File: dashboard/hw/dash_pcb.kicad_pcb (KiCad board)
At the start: 2 copper layers, 180 x 65 mm, 5 parts, among them J1 LCD, J2 DEBUG, J3 LCD_BL, U1 LPC11C24FBD48

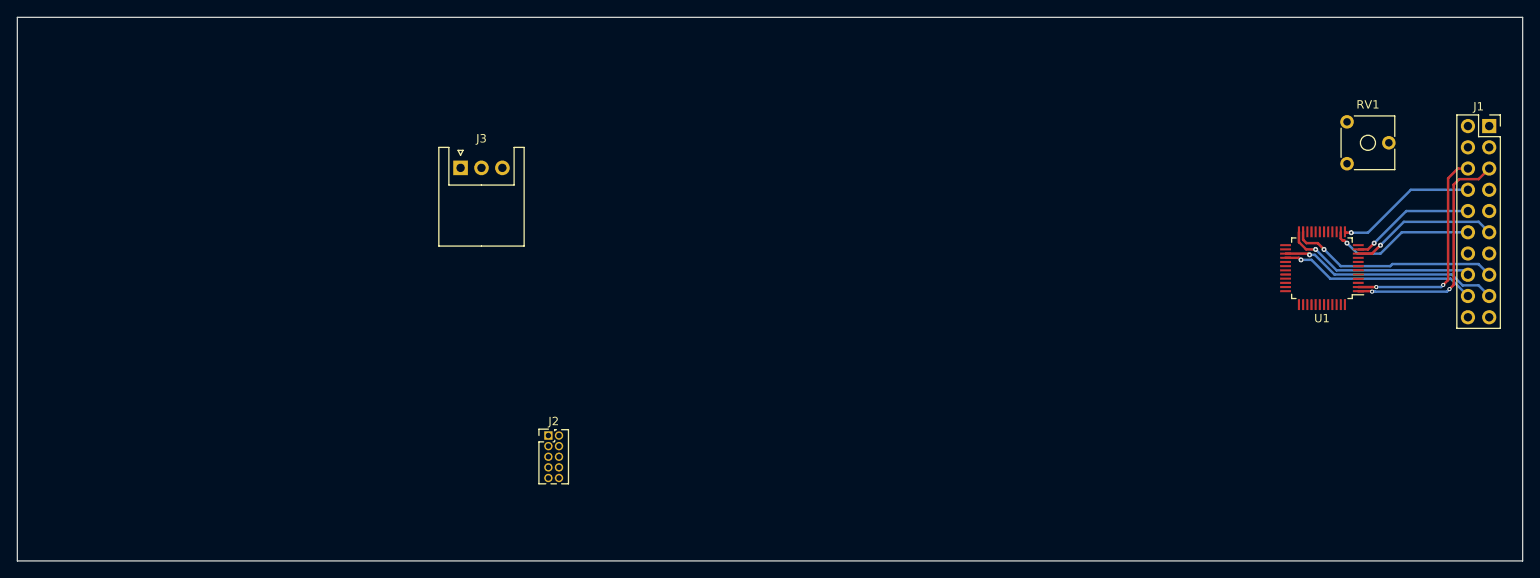
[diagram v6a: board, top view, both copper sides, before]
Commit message: place new components relatively on board
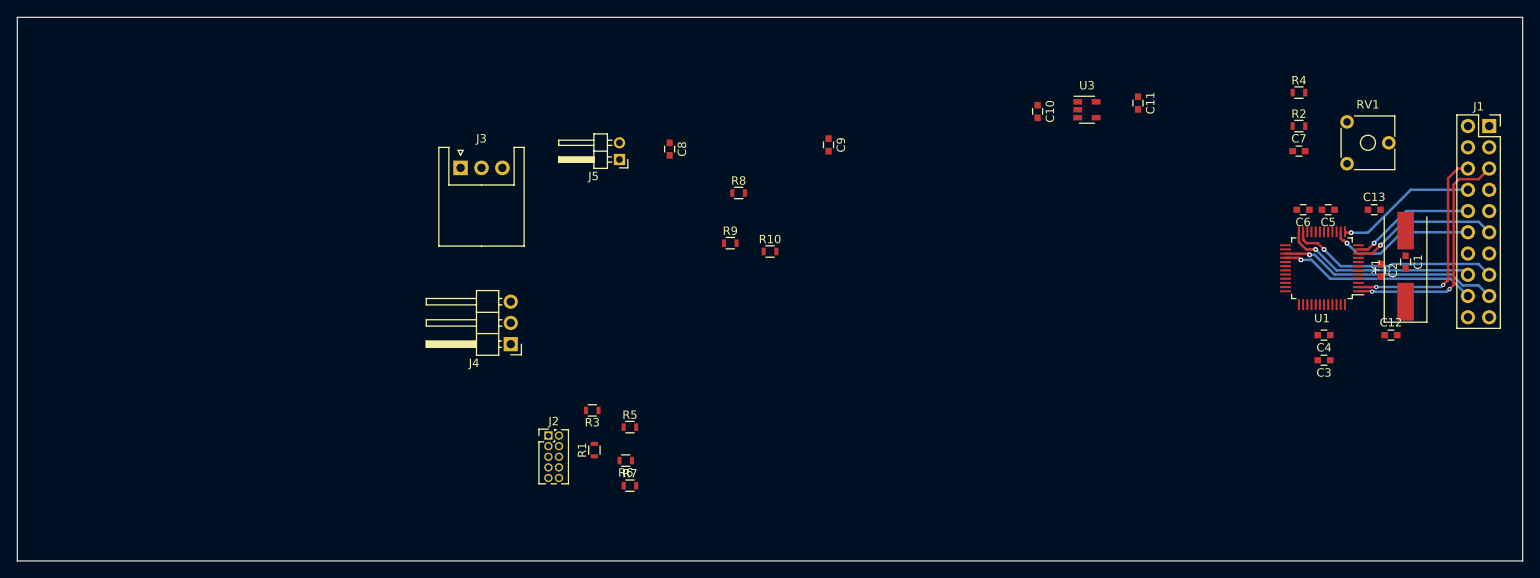
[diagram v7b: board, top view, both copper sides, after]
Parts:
- added C1: 100n, Capacitors_SMD:C_0603, F.Cu at (251.0, 84.2)
- added C10: 2.2u, Capacitors_SMD:C_0603, F.Cu at (207.0, 66.2)
- added C11: 2.2u, Capacitors_SMD:C_0603, F.Cu at (219.0, 65.2)
- added C12: 39p, Capacitors_SMD:C_0603, F.Cu at (249.2, 93.0)
- added C13: 39p, Capacitors_SMD:C_0603, F.Cu at (247.2, 78.0)
- added C2: 10n, Capacitors_SMD:C_0603, F.Cu at (248.0, 85.2)
- added C3: 100n, Capacitors_SMD:C_0603, F.Cu at (241.2, 96.0)
- added C4: 10n, Capacitors_SMD:C_0603, F.Cu at (241.2, 93.0)
- added C5: 10n, Capacitors_SMD:C_0603, F.Cu at (241.8, 78.0)
- added C6: 100n, Capacitors_SMD:C_0603, F.Cu at (238.8, 78.0)
- added C7: 1n, Capacitors_SMD:C_0603, F.Cu at (238.2, 71.0)
- added C8: 2.2u, Capacitors_SMD:C_0603, F.Cu at (163.0, 70.8)
- added C9: 22u, Capacitors_SMD:C_0603, F.Cu at (182.0, 70.2)
- added J4: CAN, Pin_Headers:Pin_Header_Angled_1x03_Pitch2.54mm, F.Cu at (144.0, 94.1)
- added J5: POWER, Pin_Headers:Pin_Header_Angled_1x02_Pitch2.00mm, F.Cu at (157.0, 72.0)
- added R1: 10k, Resistors_SMD:R_0603, F.Cu at (154.0, 106.8)
- added R10: 383k, Resistors_SMD:R_0603, F.Cu at (175.0, 83.0)
- added R2: 60, Resistors_SMD:R_0603, F.Cu at (238.2, 68.0)
- added R3: 10k, Resistors_SMD:R_0603, F.Cu at (153.8, 102.0)
- added R4: 60, Resistors_SMD:R_0603, F.Cu at (238.2, 64.0)
- added R5: 60, Resistors_SMD:R_0603, F.Cu at (158.2, 104.0)
- added R6: 60, Resistors_SMD:R_0603, F.Cu at (157.8, 108.0)
- added R7: 60, Resistors_SMD:R_0603, F.Cu at (158.2, 111.0)
- added R8: 100k, Resistors_SMD:R_0603, F.Cu at (171.2, 76.0)
- added R9: 2M, Resistors_SMD:R_0603, F.Cu at (170.2, 82.0)
- added U3: TLV70233_SOT23-5, TO_SOT_Packages_SMD:SOT-23-5, F.Cu at (212.9, 66.0)
- added Y1: 12MHz, Crystals:Crystal_SMD_HC49-SD, F.Cu at (251.0, 84.8)
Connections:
- J2 pad 10: /MCU_~RESET -> Net-(J2-Pad10)
- J2 pad 2: /SWDIO -> Net-(J2-Pad2)
- J2 pad 4: /SWCLK -> Net-(J2-Pad4)
- U1 pad 4: +3V3 -> Net-(R1-Pad1)

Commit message: more parts shopping
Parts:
- removed J5: POWER, Pin_Headers:Pin_Header_Angled_1x02_Pitch2.00mm
- added R11: 36, Resistors_SMD:R_1206, F.Cu at (188.1, 104.5)
- added R12: 36, Resistors_SMD:R_1206, F.Cu at (188.1, 108.5)
- J2: footprint Pin_Headers:Pin_Header_Straight_2x05_Pitch1.27mm -> Pin_Headers:Pin_Header_Angled_2x05_Pitch1.27mm
- J3: footprint Connectors_JST:JST_XH_S03B-XH-A_03x2.50mm_Angled -> Pin_Headers:Pin_Header_Angled_1x03_Pitch2.54mm
- J4: value CAN -> CAR; footprint Pin_Headers:Pin_Header_Angled_1x03_Pitch2.54mm -> Pin_Headers:Pin_Header_Angled_1x06_Pitch2.54mm
- RV1: footprint Potentiometers:Potentiometer_Trimmer_ACP_CA6v_Horizontal -> Potentiometers:Potentiometer_Trimmer_ACP_CA6h_Vertical
- moved J4 7.87 mm to (137.8, 98.9)
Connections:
- C8 pad 1: Net-(C8-Pad1) -> +BATT
- J3 pad 3: /LCD_LED_K -> GND
- J4 pad 1: /CANH -> +BATT
- J4 pad 2: /CANL -> GND
- U1 pad 11: /LCD_~RST -> /LCD_DB2
- U1 pad 12: Net-(U1-Pad12) -> /LCD_DB3
- U1 pad 45: /LCD_DB3 -> Net-(U1-Pad45)
- U1 pad 9: /LCD_DB2 -> /LCD_~RST
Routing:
- net /LCD_~RST: track 15.0 -> 13.9 mm
- net /LCD_DB2: track 0.00 -> 1.15 mm
